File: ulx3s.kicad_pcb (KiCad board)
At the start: 8 copper layers, 60.1 x 32 mm, 87 parts, among them J3 hub75-abcd, J4 CONN_02X03, J5 hub75-abcd, U1 LFE5U-85F-6BG381C, U10 IS25LP128F-JBLE, U11 MPM54304GMN-0001, U2 IS42S16160J-6BL, U6 FT231XS, U9 ESP32-S3-WROOM-1, Y1 ECS-1612MV-250-CN-TR

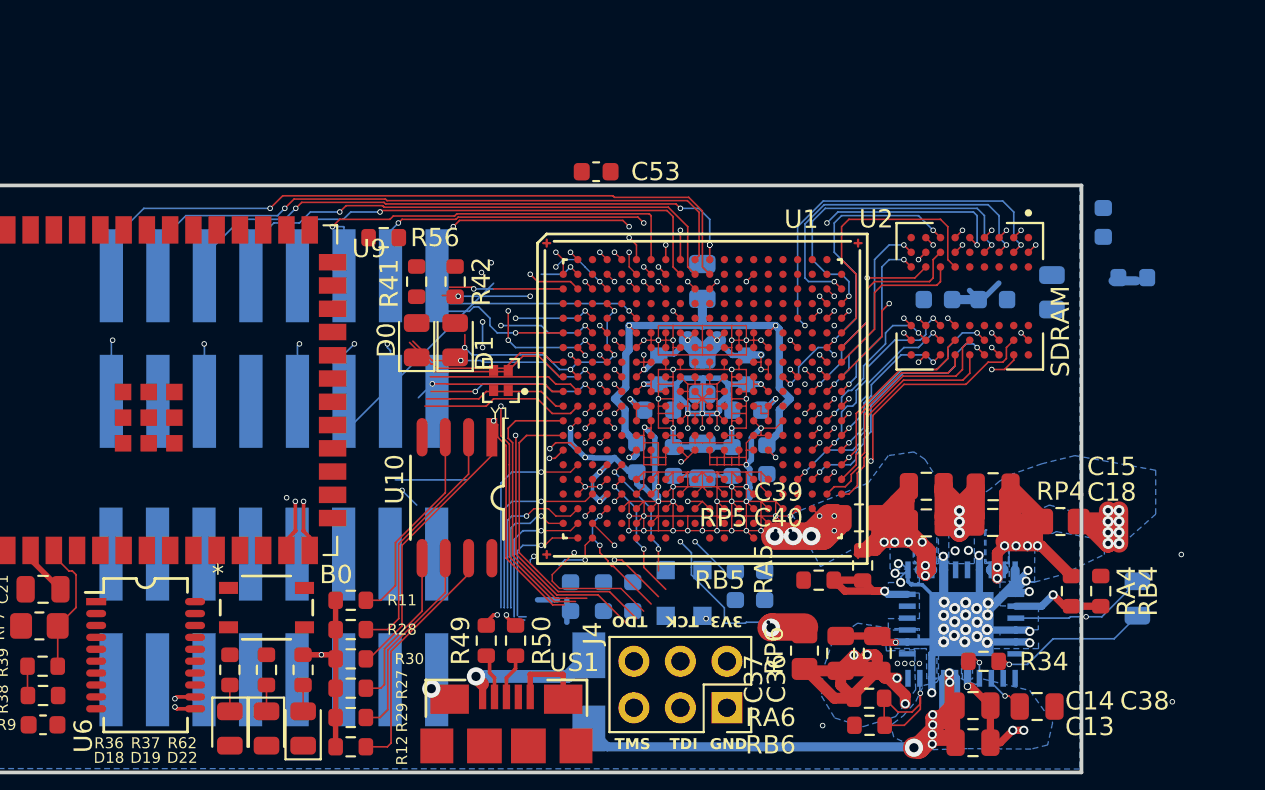
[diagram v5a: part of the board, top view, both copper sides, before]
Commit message: finished routing conn1/conn2
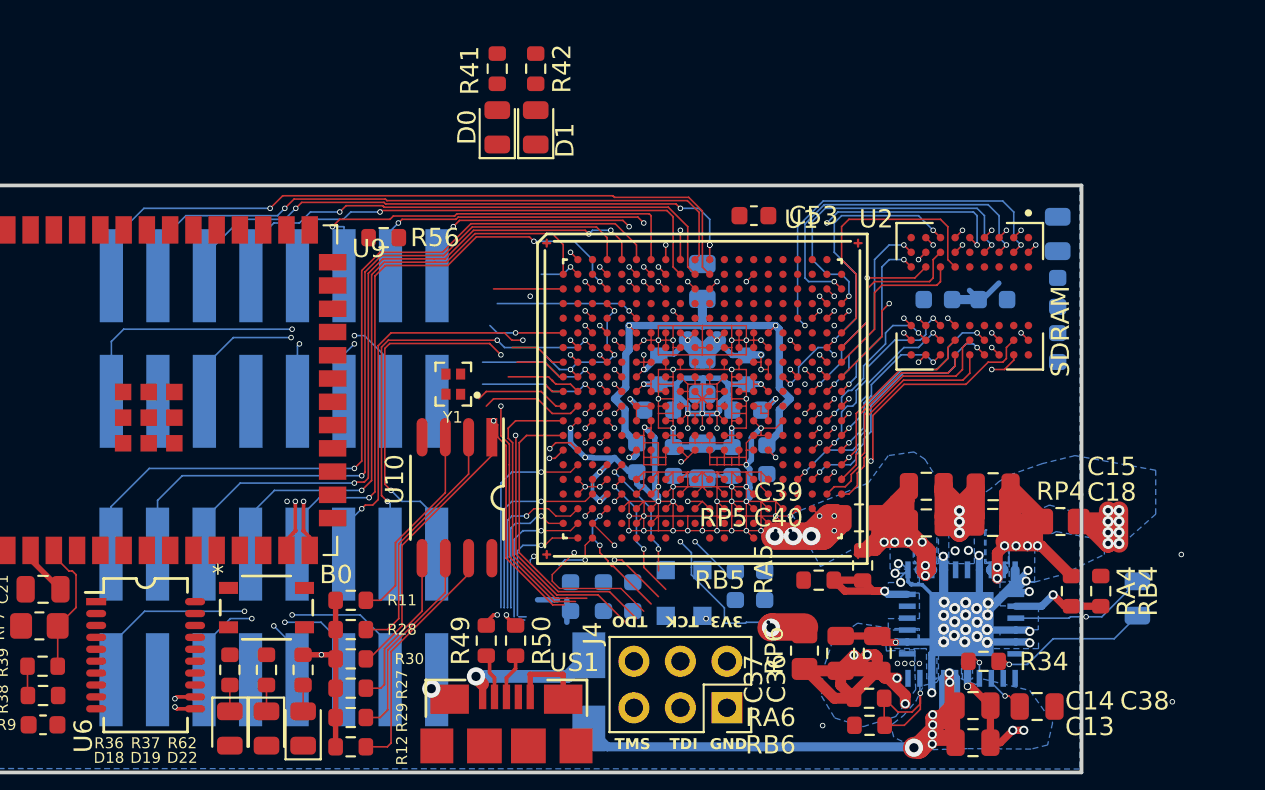
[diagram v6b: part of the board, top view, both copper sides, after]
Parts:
- moved D0 12.4 mm to (122.3, 67.6)
- moved R41 12.4 mm to (122.3, 64.4)
- moved D1 12.4 mm to (124.4, 67.6)
- moved R42 12.4 mm to (124.4, 64.4)
- moved C53 8.94 mm to (136.3, 72.4)
- moved C52 5.60 mm to (152.9, 79.6), turned to -90 degrees
- moved C35 4.56 mm to (152.9, 76.6)
- moved C16 3.20 mm to (152.9, 73.4)
- moved Y1 2.61 mm to (119.9, 81.6)
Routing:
- net GN7: track 5.97 -> 50.6 mm, vias 1 -> 2
- net GP7: track 5.64 -> 45.1 mm
- net GP8: track 3.57 -> 41.5 mm
- net GP9: track 4.08 -> 40.9 mm, vias 1 -> 2
- net GN8: track 4.71 -> 39.2 mm, vias 1 -> 3
- net GN10: track 7.22 -> 40.8 mm, vias 1 -> 2
- net GN12: track 8.78 -> 38.8 mm
- net GN9: track 4.16 -> 34.0 mm
- net GN11: track 8.77 -> 37.4 mm
- net GP10: track 6.57 -> 33.7 mm, vias 2 -> 3
- net SD_D2: track 23.9 -> 1.17 mm, vias 1 -> 0
- net GP11: track 9.35 -> 25.8 mm, vias 1 -> 3
- net GP12: track 10.4 -> 23.7 mm
- net GP13: track 13.0 -> 26.0 mm
- net WIFI_GPIO40: track 11.4 -> 5.03 mm
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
